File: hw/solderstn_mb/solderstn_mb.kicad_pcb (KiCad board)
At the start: 4 copper layers, 160 x 221.5 mm, 407 parts, among them J1201 Conn_02x05_Odd_Even, J1202 USB_B-TE_1734346-1, J1203 DB9_Male_MountingHoles, J1204 USB_A-TE_1-292303-1, J1301 SJ-3571N, J1302 Conn_02x05_Odd_Even, J201 74980104400, J2101 Conn_01x02, J2102 Molex_PicoBlade-53398-0271, J2103 CES-30207-158L120-67_Molex-Pi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, J2104 CES-703116-28PM_JST-conn, J2105 CES-30207-158L120-67_Molex-Pi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, J2106 CES-703116-28PM_JST-conn, J301 Molex_MicroFit_30-43045-0421, J501 FFC_conn_14p, J502 FFC_conn_14p, J503 Molex_MicroClasp-55935-0210, M501 FFC_retention_clamp, M502 FFC_retention_clamp, M601 Fan_4pin, M701 Fan_4pin, M801 Fan_4pin, Q1601 DMG1013T, Q1701 DMG1013T, Q1901 DMG1013T, Q2001 DMG1013T, Q2201 DMG1012T, Q301 Si4497DY, Q302 Si4497DY, Q303 DMG1012T, Q501 DMG1012T, Q601 DMG1012T, Q701 DMG1012T, Q801 DMG1012T, SW2201 Pushbutton_SMD_TS-1102W-4316, SW2202 Pushbutton_SMD_TS-1102W-4316, U1001 TMP100, U1101 TMP100, U1201 USBLC6-2SC6, U1202 74LVC2G17gw, U1203 USBLC6-2SC6, U1401 TMUX1219, U1402 TMUX1219, U1501 AD8552ARU, U1502 INA226, U1503 TPS2HB16AQ1, U1504 INA226, U1505 74LVC1G11dck, U1506 74LVC1G11dck, U1507 74LVC1G11dck, U1601 NE556d, U1602 74LVC1G175dck, U1603 74LVC1G11dck, U1701 74LVC1G175dck, U1702 74LVC1G11dck, U1801 AD8552ARU, U1802 INA226, U1803 TPS2HB16AQ1, U1804 INA226, U1805 74LVC1G11dck, U1806 74LVC1G11dck, U1807 74LVC1G11dck, U1901 NE556d, U1902 74LVC1G175dck, U1903 74LVC1G11dck, U2001 74LVC1G175dck, U2002 74LVC1G11dck, U201 IP101GA, U202 74LVC1G126SE, U2101 Si4735-D60-GU, U2102 TS4990IDT, U2103 TS4990IDT, U2201 MCP1316T-26LE-OT, U2202 W25Q64FV, U301 TPS54332DDA, U302 TLV1117LV30DCY, U303 TLV1117LV30DCY, U304 TLV1117LV30DCY, U305 AP22811AW5, U401 STM32F429VITx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

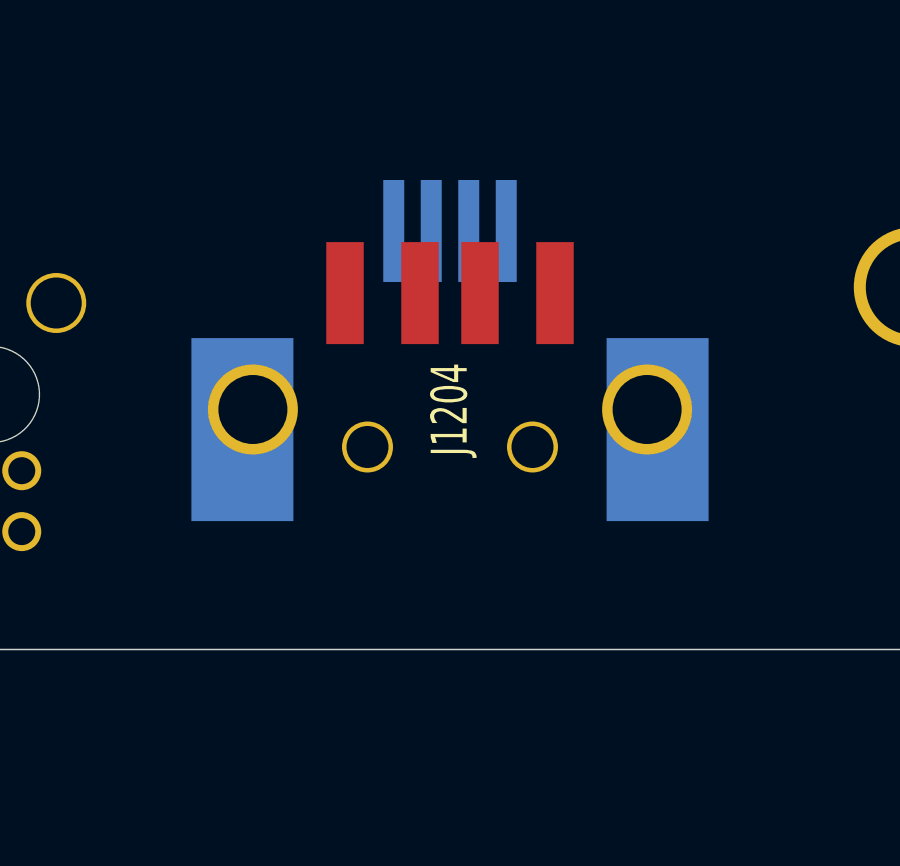
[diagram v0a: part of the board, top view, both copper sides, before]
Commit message: Updated USB-A conn to CUI UJ2-AH-1-SMT because retention pads are SMD. Also better USB-A cutout in back panel. Updated 3d test model
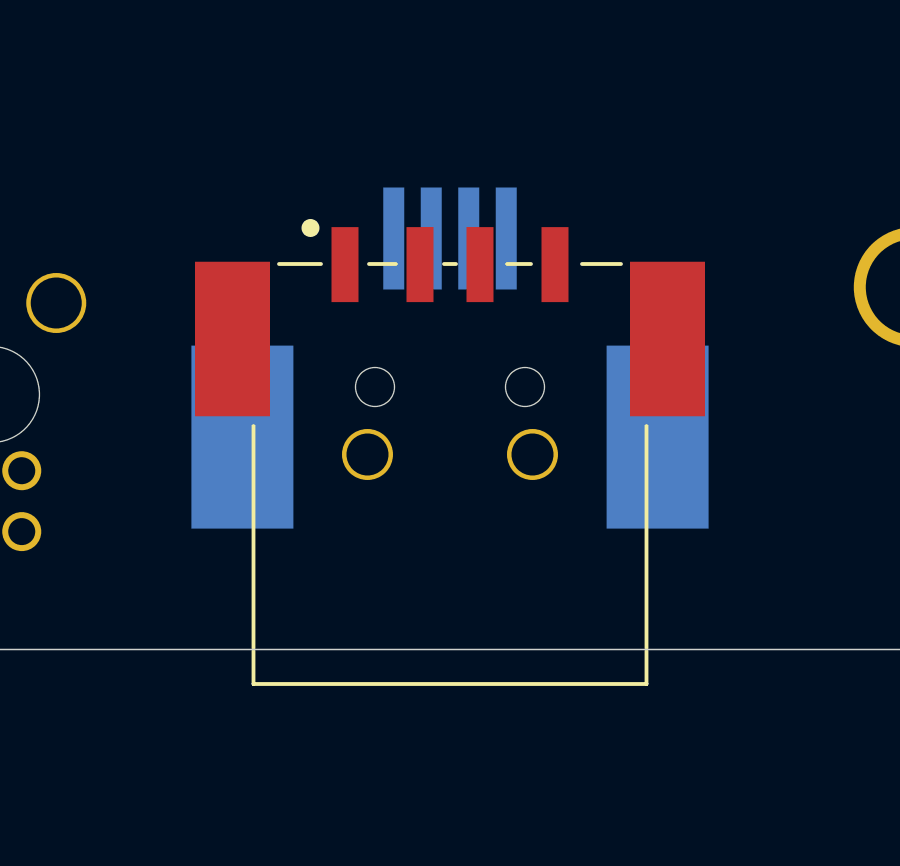
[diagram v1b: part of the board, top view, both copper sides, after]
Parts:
- J1204: value USB_A-TE_1-292303-1 -> USB_A-CUI-UJ2-AH-1-SMT; footprint customlib_mj_fp:TE_1-292303-1 -> customlib_mj_fp:CUI-UJ2_AH_1_SMT
- moved J1204 0.75 mm to (168.5, 242.8), turned to 0 degrees
- moved J1202 0.25 mm to (168.5, 245.0)

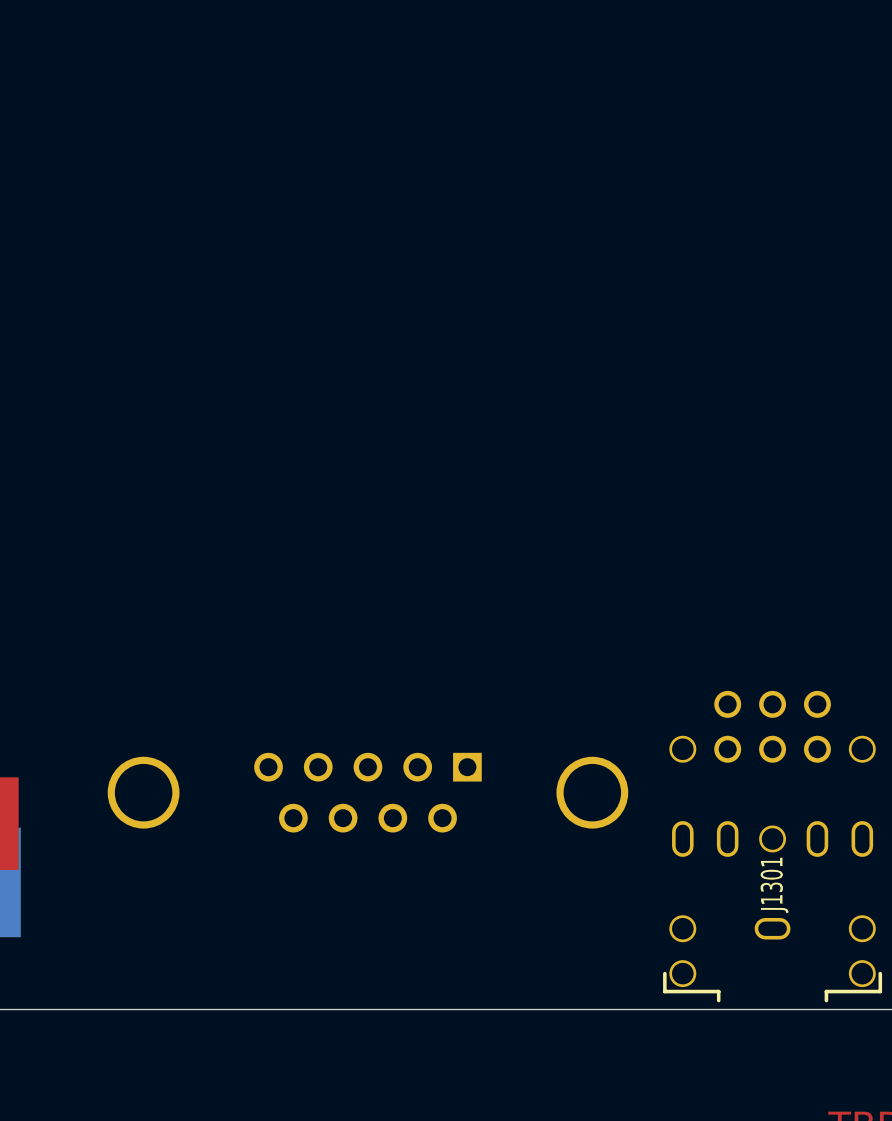
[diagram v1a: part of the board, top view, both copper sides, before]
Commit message: Add 12V DC-out (Molex Nano-Fit 1x02) and SMA in back-panel, for FM antenna & ext. ant.amp. Updated Dsub9 conn to correct component & placement on MB.
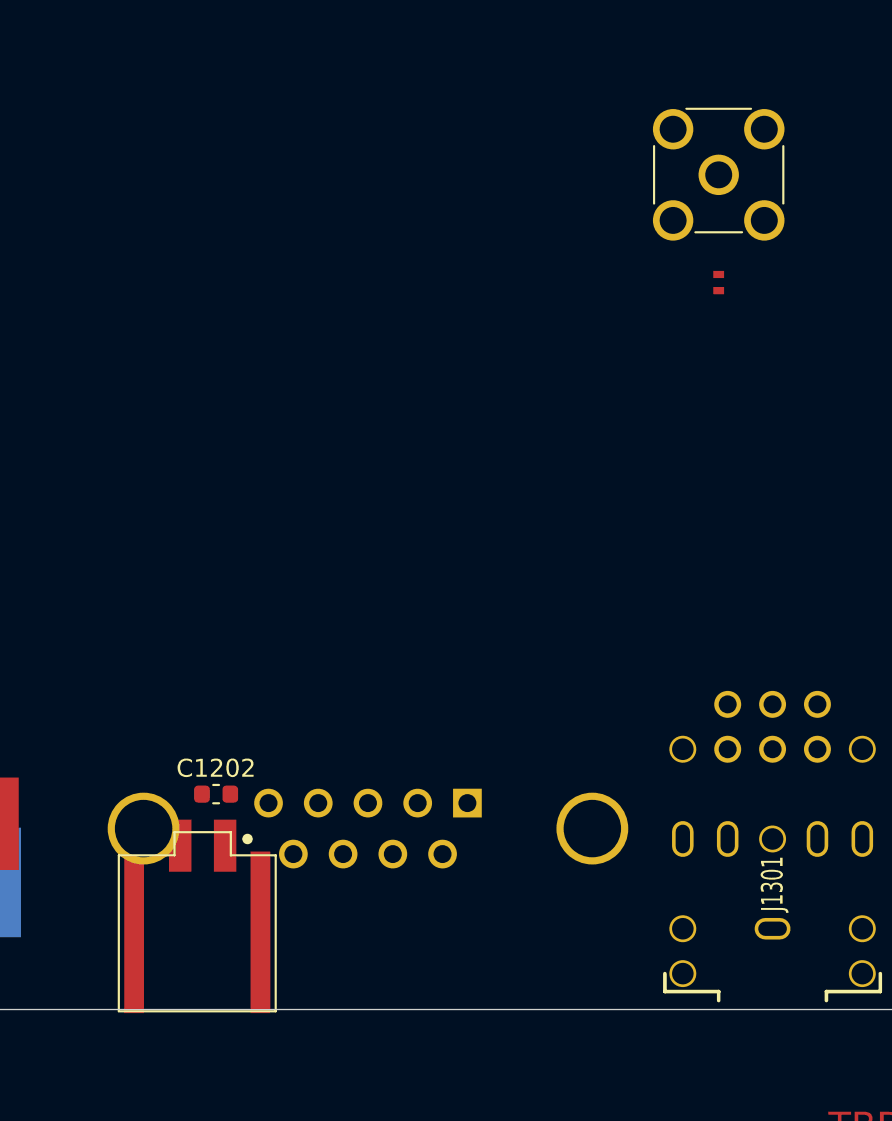
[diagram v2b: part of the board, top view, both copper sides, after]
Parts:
- added C1202: 100n, Capacitor_SMD:C_0603_1608Metric, F.Cu at (188.0, 239.5)
- added J1205: Molex_NanoFit-1x02, customlib_mj_fp:Molex_NanoFit_105430-1102_1x02_P2.50mm_Horizontal, F.Cu at (187.2, 247.5)
- added J2107: Conn_Coaxial, customlib_mj_fp:SMA_Molex_73251-2200_Horizontal, F.Cu at (216.0, 205.0)
- added JP2106: dogbone_2_ud, customlib_mj_fp:db2_ud_0402, F.Cu at (216.0, 211.0)
- J1203: footprint Connector_Dsub:DSUB-9_Male_Horizontal_P2.77x2.84mm_EdgePinOffset9.90mm_Housed_MountingHolesOffset11.32mm -> customlib_mj_fp:DSub9-Kycon_K22X-EP9P-N
- moved J1203 2.00 mm to (202.0, 240.0)
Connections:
- net Net-(C2105-Pad1) renamed /Audio & FM-radio/FMI
- J1202 pad S1: (no net) -> GND
- J1202 pad S2: (no net) -> GND

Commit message: Backpanel: move SMA to side, under MB PCB, also 12V-out moved outwards (and had to shift 12V/Gnd pins);   Mainboard: Move SMA-RA to bottomside, wont fit on Topside. ALso prelim. scatter/placement of some comps.
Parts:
- C210, C2202, C301, D2201, J2107, JP2106, Q2201, R210, R2201, R2202, RTC2201, U1201, U1401, U1402, U201, U202, Y201: moved to B.Cu
- J301: footprint Connector_Molex:Molex_Micro-Fit_3.0_43045-0421_2x02-1MP_P3.00mm_Horizontal -> customlib_mj_fp:Molex_Micro-Fit_3.0_43045-0421_2x02-1MP_P3.00mm_Horizontal
- moved U1501 333.0 mm to (174.0, 231.0)
- moved U1202 327.8 mm to (195.0, 249.0), turned to 180 degrees
- moved D1201 323.7 mm to (196.5, 246.0), turned to 180 degrees
- moved R1205 322.9 mm to (193.0, 247.0)
- moved D2201 321.5 mm to (56.0, 128.0), turned to 180 degrees
- moved Q1701 319.9 mm to (173.0, 223.0), turned to 180 degrees
- moved U1502 317.3 mm to (166.0, 206.0), turned to 180 degrees
- moved R1512 313.8 mm to (174.0, 208.0), turned to 270 degrees
- moved U1203 311.2 mm to (168.0, 234.0), turned to 270 degrees
- moved R1505 310.9 mm to (161.0, 208.0), turned to 90 degrees
- moved U1201 310.3 mm to (169.0, 233.0), turned to 270 degrees
- moved U1506 308.9 mm to (175.3, 197.7), turned to 180 degrees
- moved U1504 305.4 mm to (169.0, 210.0)
- moved U1503 301.2 mm to (168.0, 199.0)
- moved U1507 300.9 mm to (160.0, 189.0), turned to 180 degrees
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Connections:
- D1201 pad 4: Net-(D1201-Pad4) -> SWCLK
- D1201 pad 5: SWCLK -> MCU_BOOT0
- D1201 pad 6: MCU_BOOT0 -> Net-(D1201-Pad6)
- J1203 pad 3: Net-(D1201-Pad4) -> Net-(D1201-Pad6)
- J1205 pad 1: VIN -> GND
- J1205 pad 2: GND -> VIN
- R1205 pad 2: Net-(D1201-Pad4) -> Net-(D1201-Pad6)
- U1201 pad 1: USB1_DP -> USB1_DM
- U1201 pad 3: USB1_DM -> USB1_DP
- U1201 pad 4: Net-(J1202-Pad2) -> Net-(J1202-Pad3)
- U1201 pad 6: Net-(J1202-Pad3) -> Net-(J1202-Pad2)
- Y201 pad 1: Net-(C209-Pad2) -> Net-(C208-Pad2)
- Y201 pad 3: Net-(C208-Pad2) -> Net-(C209-Pad2)

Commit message: *) Add some docs (JST PH spk conn., SPI-flash, Molex NanoFit 12V backpanel conn.) *) MB cutouts for front-panel features *) Change PwrBtn LED conn. Molex MicroClasp -> JST PH2 to avoid througholes + allow bottom-side fit above MW PSU *) Moving some stuff (RTC-module, connectors) due to collisions *) Fixed some components with broken 3d-packages
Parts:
- C301, R2202, U1401, U1402: moved to F.Cu
- C302, C303, C304, C305, C311, C325, C326, C601, C602, C701, C702, C801, C802, D301, J301, JP601, JP701, JP801, L301, M601, M701, M801, Q601, Q701, Q801, R601, R602, R603, R701, R702, R703, R801, R802, R803, U301, U601, U701, U801: moved to B.Cu
- J2104, J2106: footprint Connector_JST:JST_PH_S2B-PH-SM4-TB_1x02-1MP_P2.00mm_Horizontal -> customlib_mj_fp:JST_PH_S2B-PH-SM4-TB_1x02-1MP_P2.00mm_Horizontal
- J503: value Molex_MicroClasp-55935-0210 -> JST_S2B-PH-SM4-TB; footprint Connector_Molex:Molex_MicroClasp_55935-0210_1x02_P2.00mm_Horizontal -> customlib_mj_fp:JST_PH_S2B-PH-SM4-TB_1x02-1MP_P2.00mm_Horizontal; moved to B.Cu
- Q301: footprint Package_SO:SO-8_3.9x4.9mm_P1.27mm -> customlib_mj_fp:SOIC-8_3.9x4.9mm_P1.27mm; moved to B.Cu
- Q302, U2102, U2103: footprint Package_SO:SO-8_3.9x4.9mm_P1.27mm -> customlib_mj_fp:SOIC-8_3.9x4.9mm_P1.27mm
- U2202: footprint customlib_mj_fp:w25q64_SO8-208 -> Package_SO:SOIC-8_5.275x5.275mm_P1.27mm
- moved Q701 289.7 mm to (78.0, 121.4), turned to 90 degrees
- moved JP701 289.7 mm to (73.8, 125.5), turned to 90 degrees
- moved C701 289.3 mm to (75.9, 125.0), turned to 90 degrees
- moved C702 288.7 mm to (74.2, 129.1), turned to 90 degrees
- moved R702 288.7 mm to (78.4, 125.0), turned to 90 degrees
- moved U701 288.1 mm to (81.6, 124.1), turned to 90 degrees
- moved R703 287.8 mm to (74.2, 133.2), turned to 90 degrees
- moved R701 286.9 mm to (74.2, 137.2), turned to 90 degrees
- moved M701 281.8 mm to (79.0, 129.0), turned to 270 degrees
- moved Q801 255.0 mm to (78.1, 140.3), turned to 90 degrees
- moved JP801 255.0 mm to (74.0, 144.5), turned to 90 degrees
- moved R801 254.7 mm to (76.0, 143.9), turned to 90 degrees
- moved R803 254.4 mm to (74.4, 148.1), turned to 90 degrees
- moved C801 254.4 mm to (78.6, 143.9), turned to 90 degrees
- moved U801 254.1 mm to (81.7, 143.0), turned to 90 degrees
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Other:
- outline, holes or cut-outs redrawn

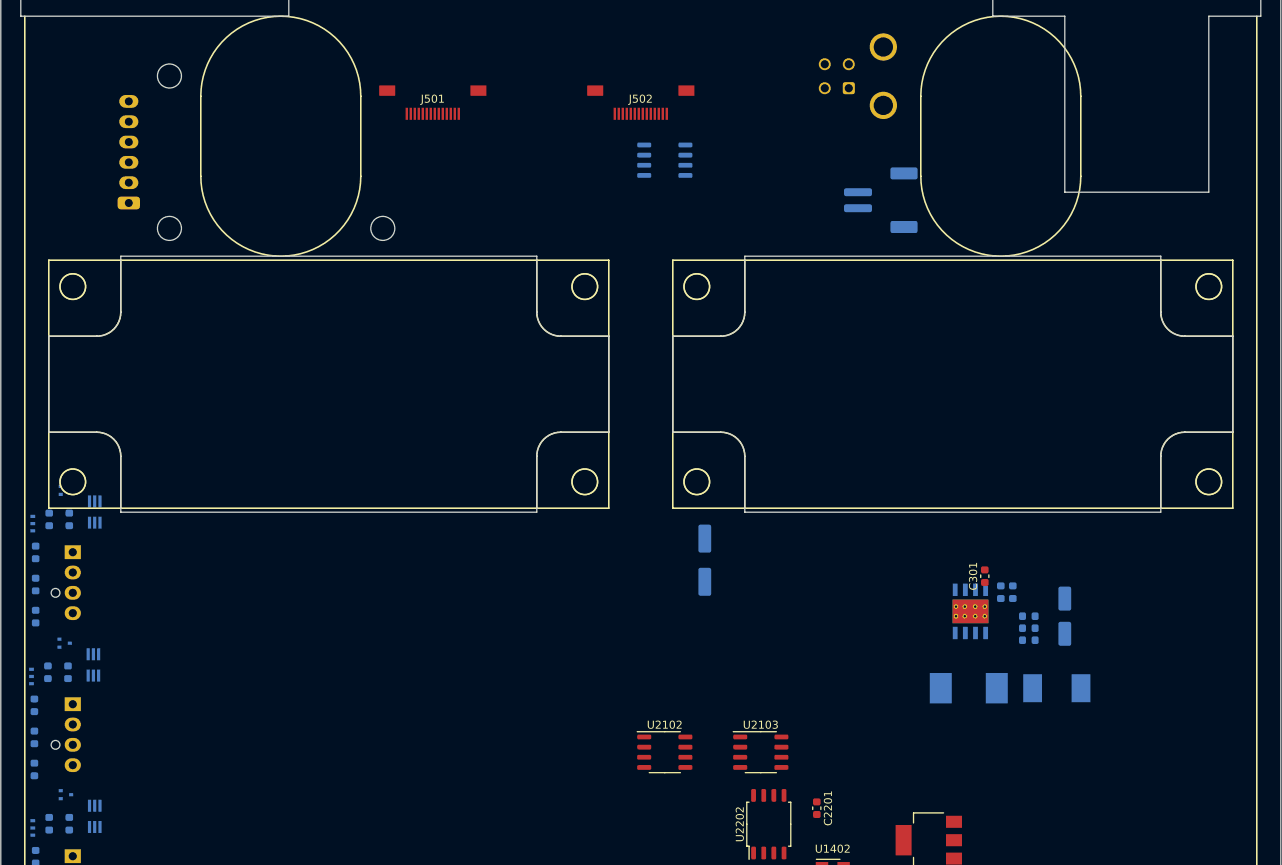
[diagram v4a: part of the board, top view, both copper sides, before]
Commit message: New alternate placement of int. speakers, RTC-mod etc.
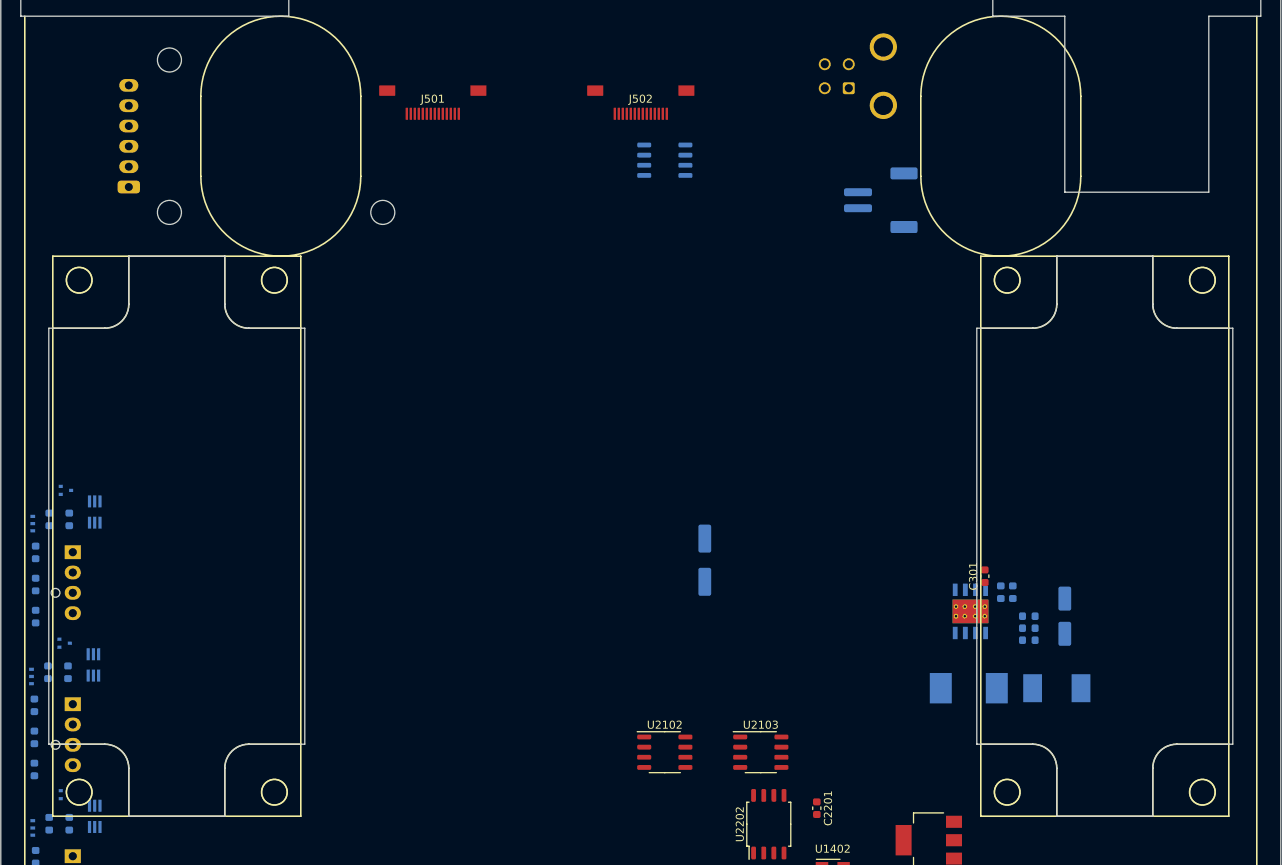
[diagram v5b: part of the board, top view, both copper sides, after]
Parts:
- moved LS2102 26.9 mm to (92.0, 108.0), turned to 0 degrees
- moved LS2104 26.9 mm to (208.0, 108.0), turned to 0 degrees
- moved RTC2201 2.00 mm to (86.0, 58.0)
- turned LS2101 to 0 degrees
- turned LS2103 to 0 degrees
